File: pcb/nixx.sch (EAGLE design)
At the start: 42 parts

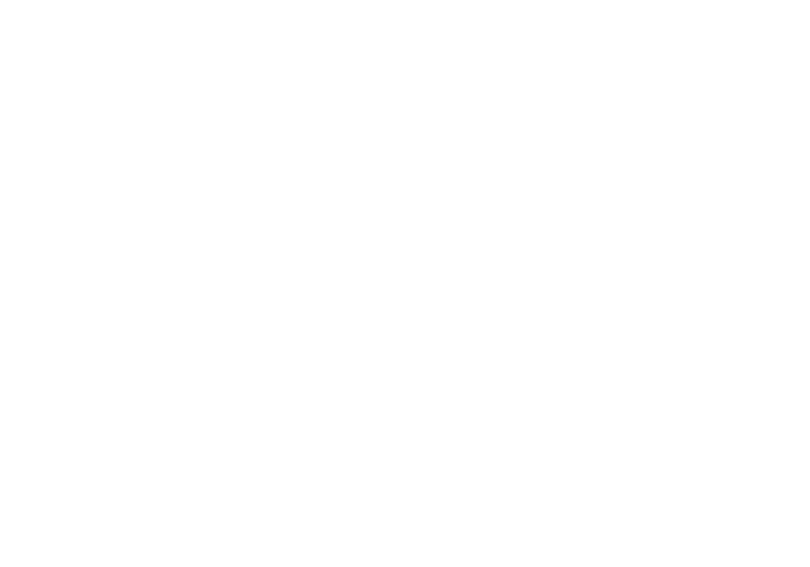
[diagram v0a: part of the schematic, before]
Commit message: added eeprom
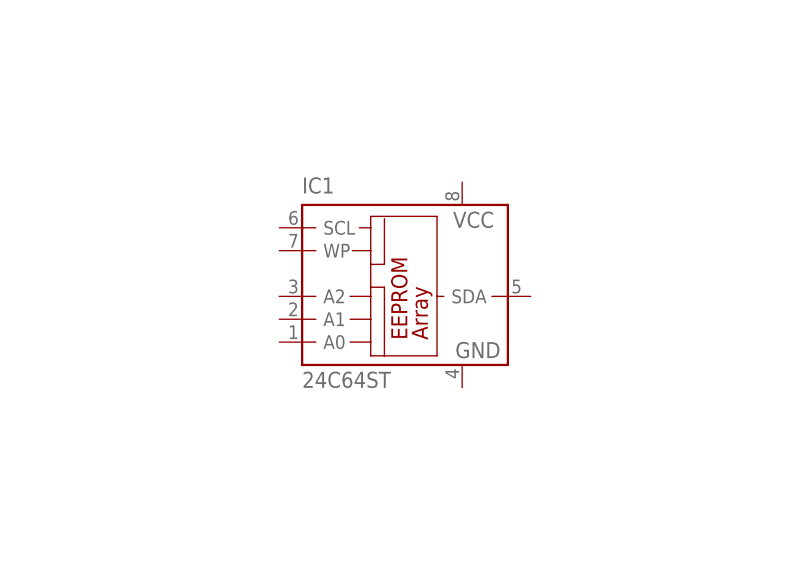
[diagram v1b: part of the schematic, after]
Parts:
- added IC1: 24C64ST, joyAnalog:24C64ST
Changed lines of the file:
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@@
 <part name="+3V6" library="joyAnalog" deviceset="+3V3" device=""/>
 <part name="C4" library="joyAnalog" deviceset="CAP" device="0805"/>
+<part name="IC1" library="joyAnalog" deviceset="24*" device="ST" technology="C64"/>
 </parts>
 <sheets>
@@
 <instance part="+3V6" gate="G$1" x="408.94" y="15.24" rot="MR0"/>
 <instance part="C4" gate="G$1" x="109.22" y="81.28"/>
+<instance part="IC1" gate="G$1" x="299.72" y="-10.16"/>
 </instances>
 <busses>

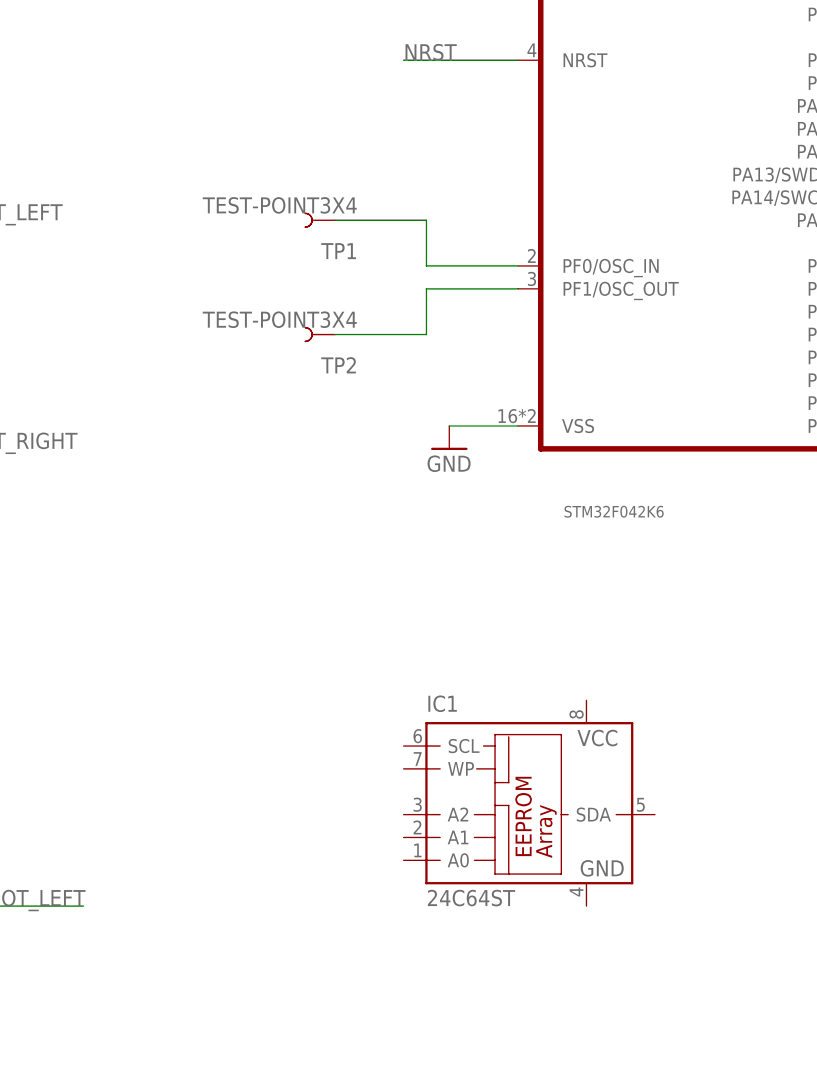
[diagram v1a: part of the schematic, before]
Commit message: added eeprom
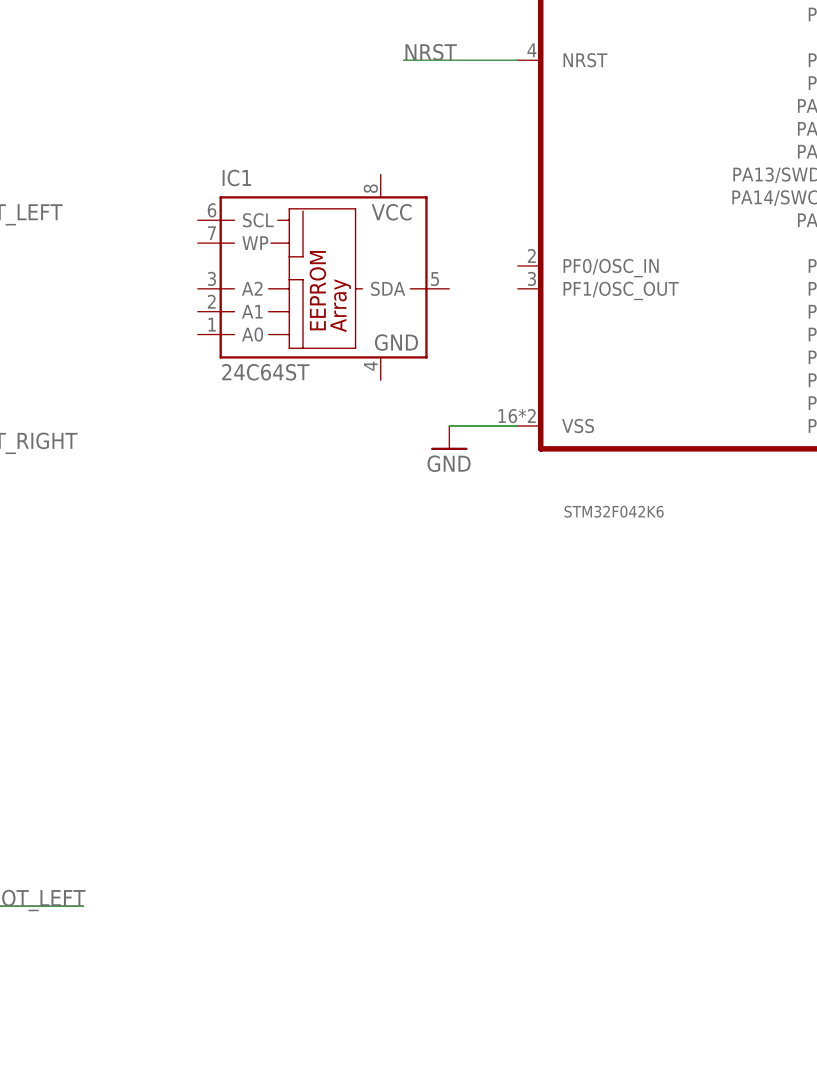
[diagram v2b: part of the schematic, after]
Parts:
- removed TP1, TP2: TEST-POINT3X4, joyAnalog:TEST-POINT3X4
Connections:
- removed net N$16: TP1.1, U$2.PF0/OSC_IN
- removed net N$18: TP2.1, U$2.PF1/OSC_OUT
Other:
- moved on the sheet: IC1
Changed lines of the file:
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@@
 <part name="R15" library="joyAnalog" deviceset="RESISTOR" device="0805-RES"/>
 <part name="R16" library="joyAnalog" deviceset="RESISTOR" device="0805-RES"/>
-<part name="TP1" library="joyAnalog" deviceset="TEST-POINT" device="3X4" value="TEST-POINT3X4"/>
-<part name="TP2" library="joyAnalog" deviceset="TEST-POINT" device="3X4" value="TEST-POINT3X4"/>
 <part name="TP3" library="joyAnalog" deviceset="TEST-POINT" device="3X4" value="TEST-POINT3X4"/>
 <part name="R17" library="joyAnalog" deviceset="RESISTOR" device="0805-RES"/>
@@
 <instance part="R15" gate="G$1" x="495.3" y="7.62"/>
 <instance part="R16" gate="G$1" x="495.3" y="-7.62"/>
-<instance part="TP1" gate="G$1" x="279.4" y="55.88" rot="R180"/>
-<instance part="TP2" gate="G$1" x="279.4" y="43.18" rot="R180"/>
 <instance part="TP3" gate="G$1" x="383.54" y="45.72"/>
 <instance part="R17" gate="G$1" x="401.32" y="17.78" rot="R90"/>
@@
 <instance part="+3V6" gate="G$1" x="408.94" y="15.24" rot="MR0"/>
 <instance part="C4" gate="G$1" x="109.22" y="81.28"/>
-<instance part="IC1" gate="G$1" x="299.72" y="-10.16"/>
+<instance part="IC1" gate="G$1" x="276.86" y="48.26"/>
 </instances>
 <busses>
@@
 </segment>
 </net>
-<net name="N$16" class="0">
-<segment>
-<pinref part="TP1" gate="G$1" pin="1"/>
-<wire x1="279.4" y1="55.88" x2="289.56" y2="55.88" width="0.1524" layer="91"/>
-<wire x1="289.56" y1="55.88" x2="289.56" y2="50.8" width="0.1524" layer="91"/>
-<pinref part="U$2" gate="G$1" pin="PF0/OSC_IN"/>
-<wire x1="289.56" y1="50.8" x2="299.72" y2="50.8" width="0.1524" layer="91"/>
-</segment>
-</net>
-<net name="N$18" class="0">
-<segment>
-<pinref part="TP2" gate="G$1" pin="1"/>
-<wire x1="279.4" y1="43.18" x2="289.56" y2="43.18" width="0.1524" layer="91"/>
-<wire x1="289.56" y1="43.18" x2="289.56" y2="48.26" width="0.1524" layer="91"/>
-<pinref part="U$2" gate="G$1" pin="PF1/OSC_OUT"/>
-<wire x1="289.56" y1="48.26" x2="299.72" y2="48.26" width="0.1524" layer="91"/>
-</segment>
-</net>

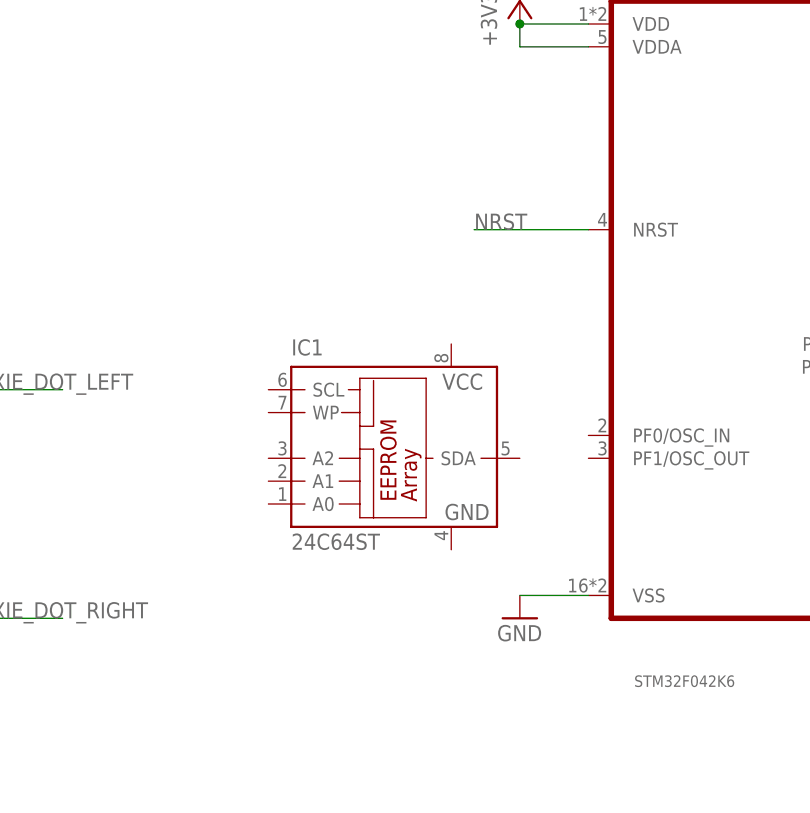
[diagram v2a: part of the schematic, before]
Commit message: added eeprom
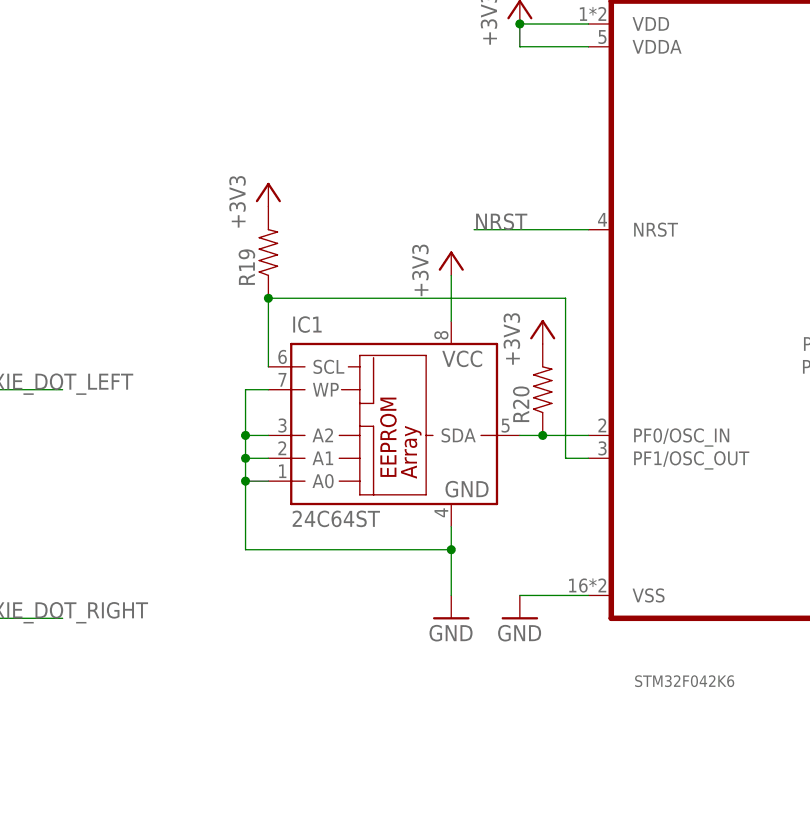
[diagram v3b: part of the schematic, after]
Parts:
- added R19, R20: (no value), joyAnalog:RESISTOR0805-RES
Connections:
- new net N$16: IC1.SDA, R20.1, U$2.PF0/OSC_IN
- new net N$18: IC1.SCL, R19.1, U$2.PF1/OSC_OUT
- net +3V3: now also IC1.VCC, R19.2, R20.2
- net GND: now also IC1.A0, IC1.A1, IC1.A2, IC1.GND, IC1.WP
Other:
- moved on the sheet: IC1
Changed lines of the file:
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@@
 <part name="C4" library="joyAnalog" deviceset="CAP" device="0805"/>
 <part name="IC1" library="joyAnalog" deviceset="24*" device="ST" technology="C64"/>
+<part name="R19" library="joyAnalog" deviceset="RESISTOR" device="0805-RES"/>
+<part name="R20" library="joyAnalog" deviceset="RESISTOR" device="0805-RES"/>
+<part name="+3V7" library="joyAnalog" deviceset="+3V3" device=""/>
+<part name="+3V8" library="joyAnalog" deviceset="+3V3" device=""/>
+<part name="GND16" library="joyAnalog" deviceset="GND" device=""/>
+<part name="+3V9" library="joyAnalog" deviceset="+3V3" device=""/>
 </parts>
 <sheets>
@@
 <instance part="+3V6" gate="G$1" x="408.94" y="15.24" rot="MR0"/>
 <instance part="C4" gate="G$1" x="109.22" y="81.28"/>
-<instance part="IC1" gate="G$1" x="276.86" y="48.26"/>
+<instance part="IC1" gate="G$1" x="276.86" y="50.8"/>
+<instance part="R19" gate="G$1" x="264.16" y="71.12" rot="R90"/>
+<instance part="R20" gate="G$1" x="294.64" y="55.88" rot="R90"/>
+<instance part="+3V7" gate="G$1" x="264.16" y="78.74"/>
+<instance part="+3V8" gate="G$1" x="294.64" y="63.5"/>
+<instance part="GND16" gate="1" x="284.48" y="30.48"/>
+<instance part="+3V9" gate="G$1" x="284.48" y="71.12"/>
 </instances>
 <busses>
@@
 <junction x="391.16" y="-43.18"/>
 </segment>
+<segment>
+<pinref part="IC1" gate="G$1" pin="GND"/>
+<pinref part="GND16" gate="1" pin="GND"/>
+<wire x1="284.48" y1="40.64" x2="284.48" y2="38.1" width="0.1524" layer="91"/>
+<pinref part="IC1" gate="G$1" pin="WP"/>
+<wire x1="284.48" y1="38.1" x2="284.48" y2="33.02" width="0.1524" layer="91"/>
+<wire x1="264.16" y1="55.88" x2="261.62" y2="55.88" width="0.1524" layer="91"/>
+<wire x1="261.62" y1="55.88" x2="261.62" y2="50.8" width="0.1524" layer="91"/>
+<pinref part="IC1" gate="G$1" pin="A0"/>
+<wire x1="261.62" y1="50.8" x2="261.62" y2="48.26" width="0.1524" layer="91"/>
+<wire x1="261.62" y1="48.26" x2="261.62" y2="45.72" width="0.1524" layer="91"/>
+<wire x1="261.62" y1="45.72" x2="264.16" y2="45.72" width="0.1524" layer="91"/>
+<pinref part="IC1" gate="G$1" pin="A1"/>
+<wire x1="264.16" y1="48.26" x2="261.62" y2="48.26" width="0.1524" layer="91"/>
+<junction x="261.62" y="48.26"/>
+<pinref part="IC1" gate="G$1" pin="A2"/>
+<wire x1="264.16" y1="50.8" x2="261.62" y2="50.8" width="0.1524" layer="91"/>
+<junction x="261.62" y="50.8"/>
+<wire x1="261.62" y1="45.72" x2="261.62" y2="38.1" width="0.1524" layer="91"/>
+<junction x="261.62" y="45.72"/>
+<wire x1="261.62" y1="38.1" x2="284.48" y2="38.1" width="0.1524" layer="91"/>
+<junction x="284.48" y="38.1"/>
+</segment>
 </net>
 <net name="N$1" class="0">
@@
 <wire x1="391.16" y1="-35.56" x2="401.32" y2="-35.56" width="0.1524" layer="91"/>
 </segment>
+<segment>
+<pinref part="R19" gate="G$1" pin="2"/>
+<pinref part="+3V7" gate="G$1" pin="+3V3"/>
+</segment>
+<segment>
+<pinref part="R20" gate="G$1" pin="2"/>
+<pinref part="+3V8" gate="G$1" pin="+3V3"/>
+</segment>
+<segment>
+<pinref part="IC1" gate="G$1" pin="VCC"/>
+<pinref part="+3V9" gate="G$1" pin="+3V3"/>
+<wire x1="284.48" y1="68.58" x2="284.48" y2="63.5" width="0.1524" layer="91"/>
+</segment>
 </net>
 <net name="SPI_SCK" class="0">
@@
 </segment>
 </net>
+<net name="N$16" class="0">
+<segment>
+<pinref part="IC1" gate="G$1" pin="SDA"/>
+<pinref part="U$2" gate="G$1" pin="PF0/OSC_IN"/>
+<wire x1="292.1" y1="50.8" x2="294.64" y2="50.8" width="0.1524" layer="91"/>
+<pinref part="R20" gate="G$1" pin="1"/>
+<wire x1="294.64" y1="50.8" x2="299.72" y2="50.8" width="0.1524" layer="91"/>
+<junction x="294.64" y="50.8"/>
+</segment>
+</net>
+<net name="N$18" class="0">
+<segment>
+<pinref part="IC1" gate="G$1" pin="SCL"/>
+<wire x1="264.16" y1="58.42" x2="264.16" y2="66.04" width="0.1524" layer="91"/>
+<wire x1="264.16" y1="66.04" x2="297.18" y2="66.04" width="0.1524" layer="91"/>
+<wire x1="297.18" y1="66.04" x2="297.18" y2="48.26" width="0.1524" layer="91"/>
+<pinref part="U$2" gate="G$1" pin="PF1/OSC_OUT"/>
+<wire x1="297.18" y1="48.26" x2="299.72" y2="48.26" width="0.1524" layer="91"/>
+<pinref part="R19" gate="G$1" pin="1"/>
+<junction x="264.16" y="66.04"/>
+</segment>
+</net>

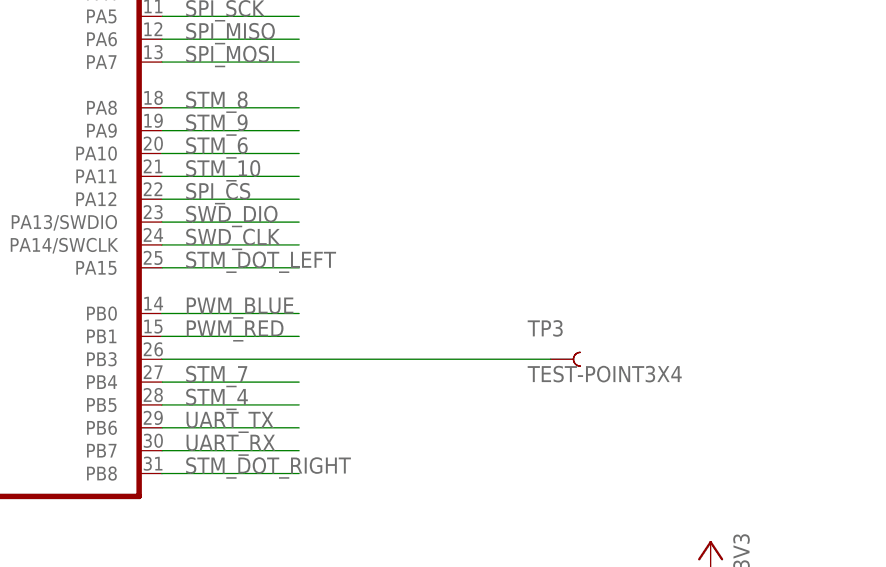
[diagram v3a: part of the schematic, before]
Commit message: using NSS, SPI test
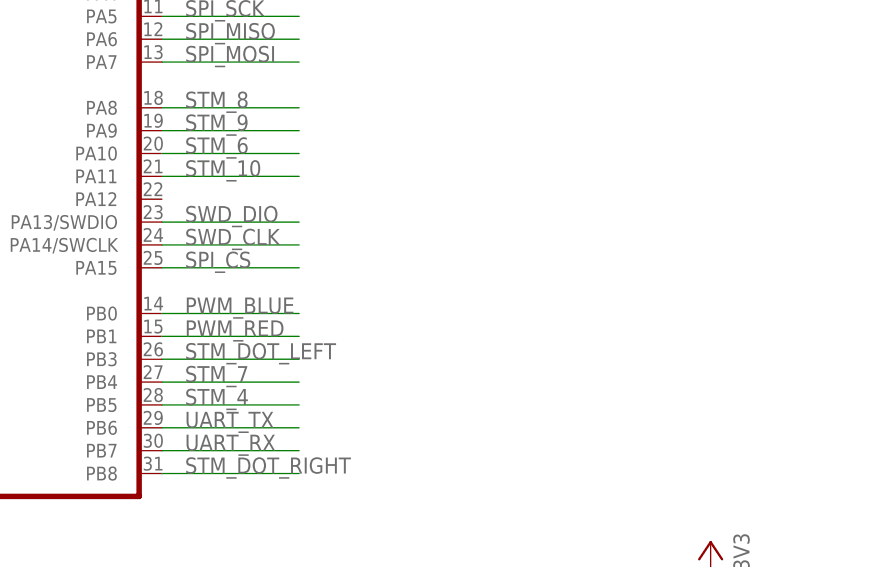
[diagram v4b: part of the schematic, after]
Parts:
- removed TP3: TEST-POINT3X4, joyAnalog:TEST-POINT3X4
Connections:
- removed net N$17: TP3.1, U$2.PB3
- net SPI_CS: now also U$2.PA15; no longer U$2.PA12
- net STM_DOT_LEFT: now also U$2.PB3; no longer U$2.PA15
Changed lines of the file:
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@@
 <part name="R15" library="joyAnalog" deviceset="RESISTOR" device="0805-RES"/>
 <part name="R16" library="joyAnalog" deviceset="RESISTOR" device="0805-RES"/>
-<part name="TP3" library="joyAnalog" deviceset="TEST-POINT" device="3X4" value="TEST-POINT3X4"/>
 <part name="R17" library="joyAnalog" deviceset="RESISTOR" device="0805-RES"/>
 <part name="R18" library="joyAnalog" deviceset="RESISTOR" device="0805-RES"/>
@@
 <instance part="R15" gate="G$1" x="495.3" y="7.62"/>
 <instance part="R16" gate="G$1" x="495.3" y="-7.62"/>
-<instance part="TP3" gate="G$1" x="383.54" y="45.72"/>
 <instance part="R17" gate="G$1" x="401.32" y="17.78" rot="R90"/>
 <instance part="R18" gate="G$1" x="408.94" y="7.62" rot="R90"/>
@@
 </segment>
 <segment>
-<pinref part="U$2" gate="G$1" pin="PA12"/>
-<wire x1="355.6" y1="63.5" x2="340.36" y2="63.5" width="0.1524" layer="91"/>
-<label x="342.9" y="63.5" size="1.778" layer="95"/>
+<label x="342.9" y="55.88" size="1.778" layer="95"/>
+<pinref part="U$2" gate="G$1" pin="PA15"/>
+<wire x1="355.6" y1="55.88" x2="340.36" y2="55.88" width="0.1524" layer="91"/>
 </segment>
 </net>
@@
 </segment>
 <segment>
-<pinref part="U$2" gate="G$1" pin="PA15"/>
-<wire x1="355.6" y1="55.88" x2="340.36" y2="55.88" width="0.1524" layer="91"/>
-<label x="342.9" y="55.88" size="1.778" layer="95"/>
+<label x="342.9" y="45.72" size="1.778" layer="95"/>
+<pinref part="U$2" gate="G$1" pin="PB3"/>
+<wire x1="355.6" y1="45.72" x2="340.36" y2="45.72" width="0.1524" layer="91"/>
 </segment>
 </net>
@@
 </segment>
 </net>
-<net name="N$17" class="0">
-<segment>
-<pinref part="U$2" gate="G$1" pin="PB3"/>
-<wire x1="383.54" y1="45.72" x2="340.36" y2="45.72" width="0.1524" layer="91"/>
-<pinref part="TP3" gate="G$1" pin="1"/>
-</segment>
-</net>

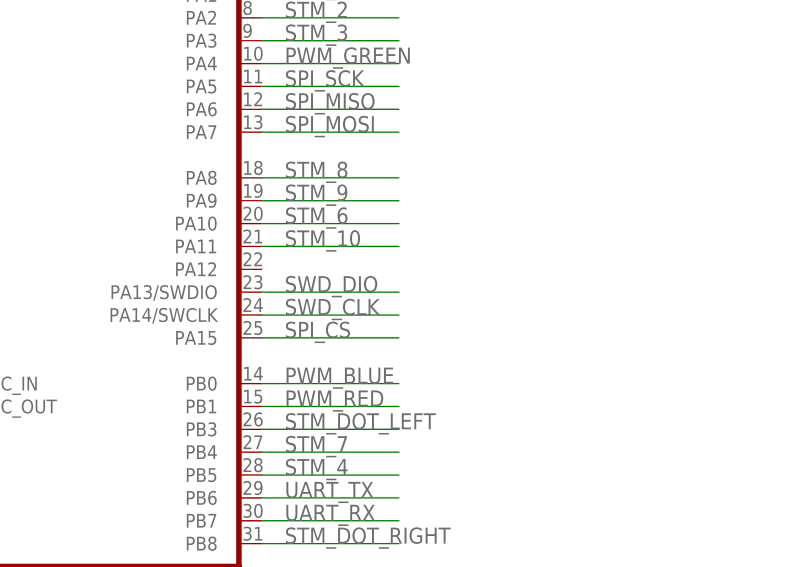
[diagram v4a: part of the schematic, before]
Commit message: PA12 testpoint
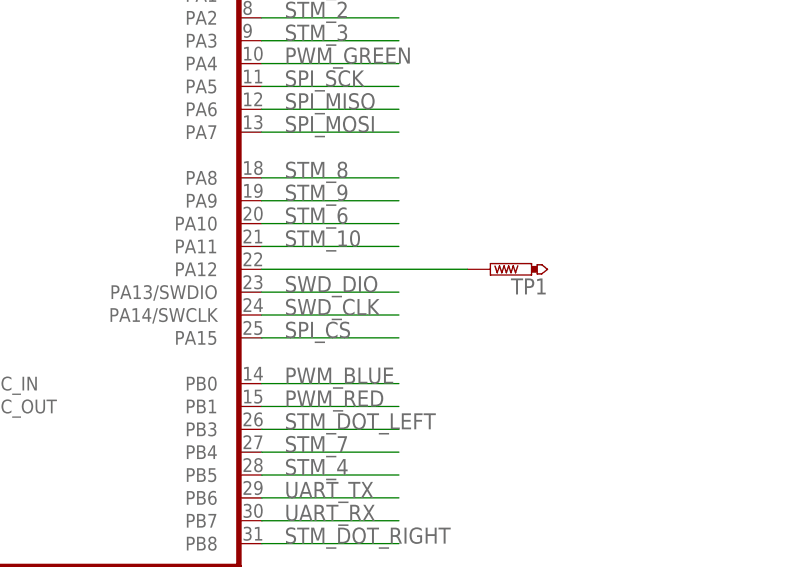
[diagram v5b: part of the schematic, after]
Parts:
- added TP1: PTR1TP13R, testpad:PTR1TP13R
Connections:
- new net N$17: TP1.TP, U$2.PA12
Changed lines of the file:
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@@
 <part name="GND16" library="joyAnalog" deviceset="GND" device=""/>
 <part name="+3V9" library="joyAnalog" deviceset="+3V3" device=""/>
+<part name="TP1" library="testpad" deviceset="PTR1" device="TP13R" value="PTR1TP13R"/>
 </parts>
 <sheets>
@@
 <instance part="GND16" gate="1" x="284.48" y="30.48"/>
 <instance part="+3V9" gate="G$1" x="284.48" y="71.12"/>
+<instance part="TP1" gate="G$1" x="365.76" y="63.5" rot="R90"/>
 </instances>
 <busses>
@@
 </segment>
 </net>
+<net name="N$17" class="0">
+<segment>
+<pinref part="U$2" gate="G$1" pin="PA12"/>
+<pinref part="TP1" gate="G$1" pin="TP"/>
+<wire x1="363.22" y1="63.5" x2="340.36" y2="63.5" width="0.1524" layer="91"/>
+</segment>
+</net>
